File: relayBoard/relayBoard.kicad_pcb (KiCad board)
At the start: 4 copper layers, 220.7 x 245.6 mm, 517 parts, among them IC1 ADUM1251, J1 Conn_01x01, J10 Conn_02x04_Top_Bottom, J11 Conn_02x04_Top_Bottom, J12 Conn_02x04_Top_Bottom, J13 Conn_02x07_Odd_Even, J14 Conn_02x07_Odd_Even, J2 Conn_01x01, J3 Conn_01x01, J4 Conn_01x01, J5 Conn_01x01, J6 Conn_01x01, J7 Conn_02x04_Top_Bottom, J8 Conn_02x04_Top_Bottom, J9 Conn_02x04_Top_Bottom, K1 G6S-2 DC12, K10 G6S-2 DC12, K11 G6S-2 DC12, K12 G6S-2 DC12, K13 G6S-2 DC12, K14 G6S-2 DC12, K15 G6S-2 DC12, K16 G6S-2 DC12, K17 G6S-2 DC12, K18 G6S-2 DC12, K19 G6S-2 DC12, K2 G6S-2 DC12, K20 G6S-2 DC12, K21 G6S-2 DC12, K22 G6S-2 DC12, K23 G6S-2 DC12, K24 G6S-2 DC12, K25 G6S-2 DC12, K26 G6S-2 DC12, K27 G6S-2 DC12, K28 G6S-2 DC12, K29 G6S-2 DC12, K3 G6S-2 DC12, K30 G6S-2 DC12, K31 G6S-2 DC12, K32 G6S-2 DC12, K33 G6S-2 DC12, K34 G6S-2 DC12, K35 G6S-2 DC12, K36 G6S-2 DC12, K37 G6S-2 DC12, K38 G6S-2 DC12, K39 G6S-2 DC12, K4 G6S-2 DC12, K40 G6S-2 DC12, K41 G6S-2 DC12, K42 G6S-2 DC12, K43 CPC1777J, K44 CPC1777J, K45 CPC1777J, K46 CPC1777J, K47 CPC1777J, K48 CPC1777J, K49 CPC1777J, K5 G6S-2 DC12, K50 CPC1777J, K51 CPC1777J, K52 CPC1777J, K53 CPC1777J, K54 CPC1777J, K55 CPC1777J, K56 CPC1777J, K57 CPC1777J, K58 CPC1777J, K59 CPC1777J, K6 G6S-2 DC12, K60 CPC1777J, K61 CPC1777J, K62 CPC1777J, K63 CPC1777J, K7 G6S-2 DC12, K8 G6S-2 DC12, K9 G6S-2 DC12, Q1 2N7002, Q10 2N7002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

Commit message: Cuyler's revisions to the relay board
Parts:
- moved D148 19.4 mm to (107.8, -33.2), turned to 270 degrees
- moved C52 9.27 mm to (110.2, -37.5), turned to 90 degrees
- moved D149 9.18 mm to (108.1, -40.1), turned to 90 degrees
- moved R176 4.93 mm to (110.2, -40.5), turned to 90 degrees
- moved R177 4.77 mm to (150.6, -37.5)
- moved R178 4.75 mm to (152.1, -37.5)
- moved D150 4.71 mm to (150.8, -34.3), turned to 270 degrees
- moved C50 1.70 mm to (92.4, -37.1)
- moved R175 1.70 mm to (101.5, -34.3)
- moved U7 1.70 mm to (99.7, -38.4)
- moved C51 1.70 mm to (97.2, -34.3)
- moved R173 1.39 mm to (100.8, -41.8)
- moved U6 0.86 mm to (142.9, -37.8)
- moved R174 0.27 mm to (104.2, -37.6), turned to 270 degrees
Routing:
- net Net-(D149-Pad2): track 24.1 -> 4.22 mm
- net +12V: track 237.3 -> 225.2 mm, vias 95 -> 97
- net /INPUT_2: track 32.0 -> 28.4 mm
- net /Sheet5F711699/GATE_SUP: track 0.00 -> 3.36 mm
- net Net-(R177-Pad1): track 9.75 -> 6.98 mm
- net GND: track 466.1 -> 463.4 mm, vias 149 -> 151
- net Net-(D148-Pad1): track 6.55 -> 4.26 mm
- net Net-(R173-Pad2): track 4.05 -> 1.85 mm
- net Net-(C52-Pad2): track 3.45 -> 1.41 mm
- net Net-(R173-Pad1): track 13.5 -> 11.5 mm
- net Net-(D150-Pad1): track 2.65 -> 1.57 mm
- net Net-(R174-Pad1): track 2.76 -> 1.96 mm
- added copper zone on F.Cu, net Net-(D149-Pad2)
- added copper zone on F.Cu, net Net-(D150-Pad2)
- added copper zone on F.Cu, net Net-(D151-Pad2)
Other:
- board text added: "Cells 1-6"
- board text added: "Cells 13-18"
- board text added: "Cells 7-12"

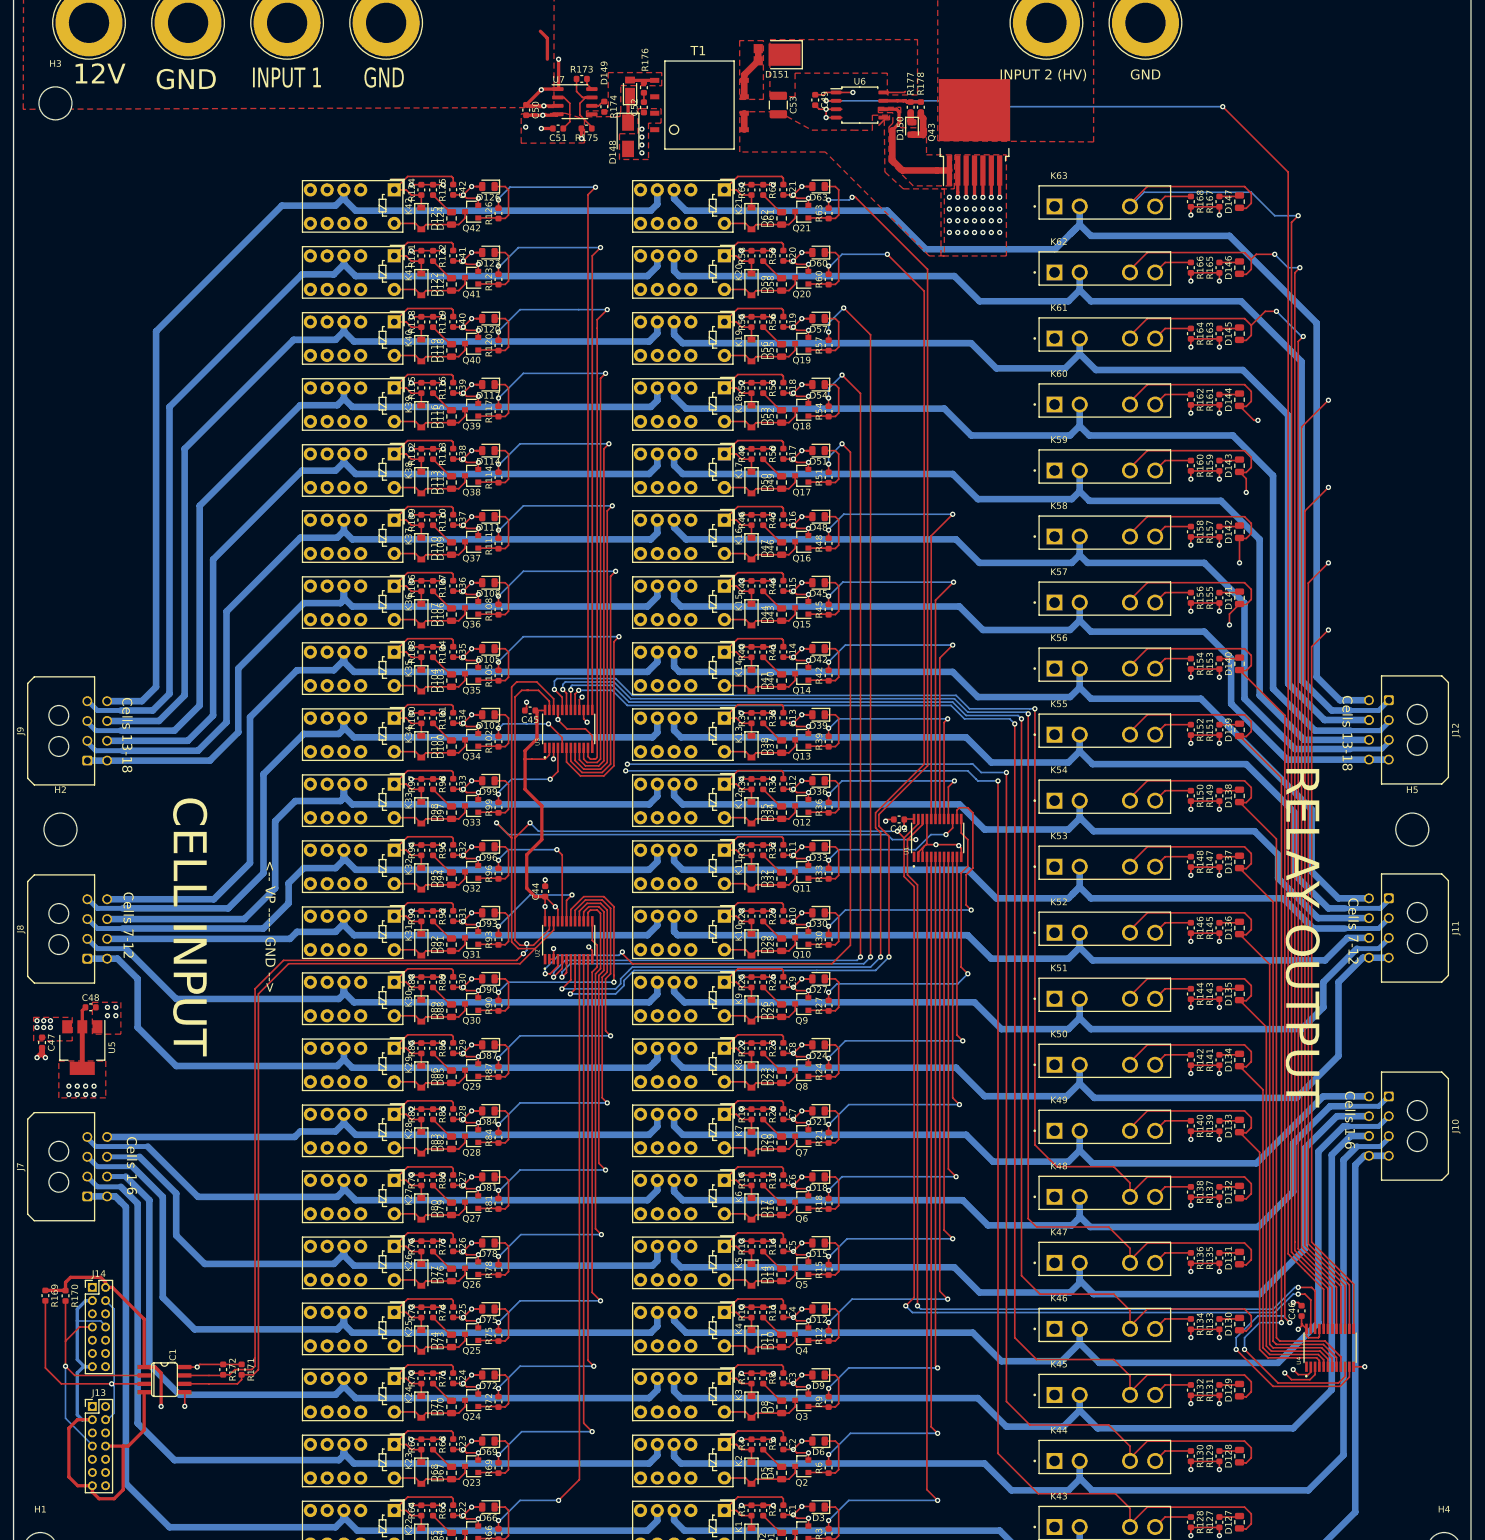
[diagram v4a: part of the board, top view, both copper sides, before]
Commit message: updates to connector connections and converter transformer
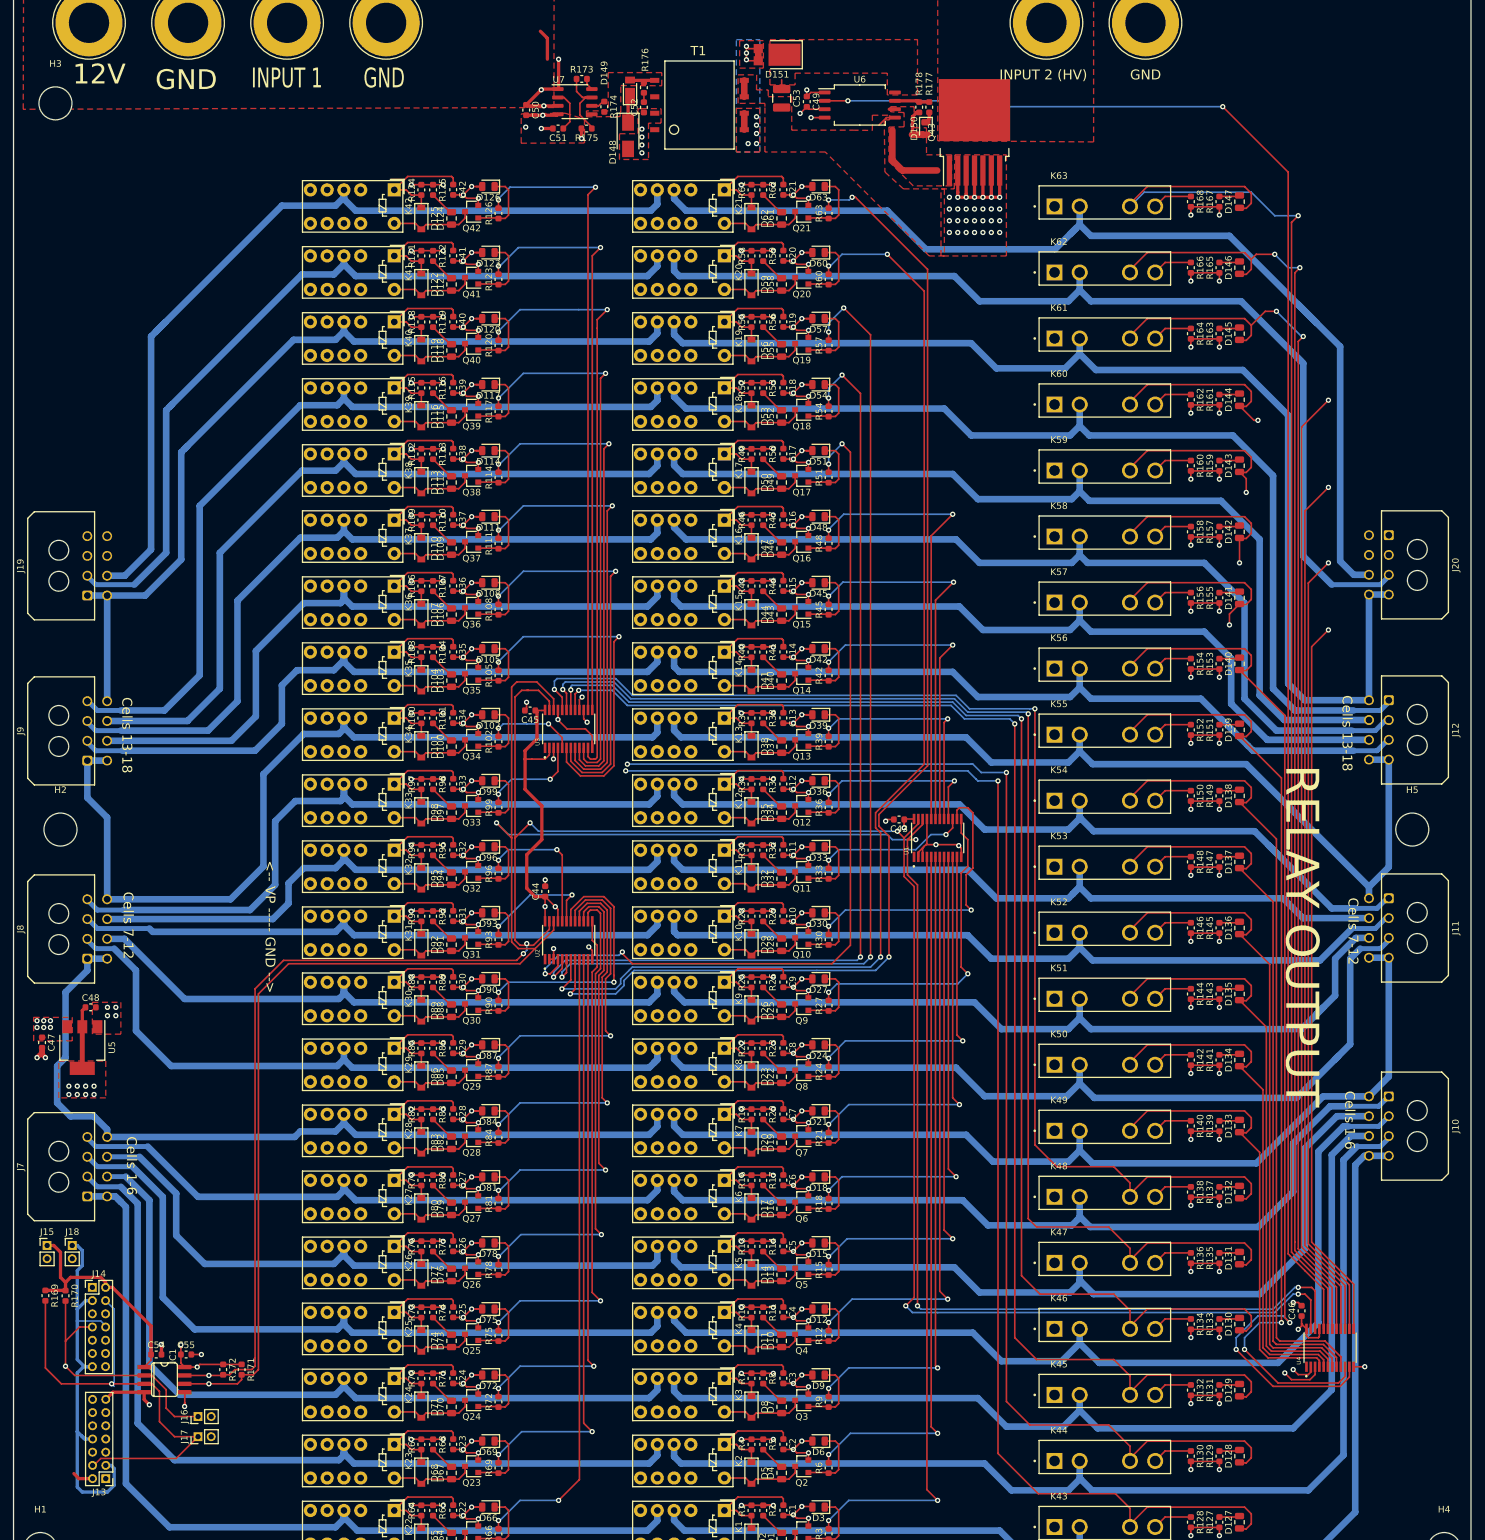
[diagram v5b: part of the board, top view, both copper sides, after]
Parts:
- added C54: 100n, Resistor_SMD:R_0603_1608Metric, F.Cu at (36.3, 151.4)
- added C55: 100n, Resistor_SMD:R_0603_1608Metric, F.Cu at (40.9, 151.4)
- added J15: Conn_01x02, Connector_PinHeader_2.00mm:PinHeader_1x02_P2.00mm_Vertical, F.Cu at (19.8, 134.9)
- added J16: Conn_01x02, Connector_PinHeader_2.00mm:PinHeader_1x02_P2.00mm_Vertical, F.Cu at (42.7, 160.8)
- added J17: Conn_01x02, Connector_PinHeader_2.00mm:PinHeader_1x02_P2.00mm_Vertical, F.Cu at (42.7, 163.8)
- added J18: Conn_01x02, Connector_PinHeader_2.00mm:PinHeader_1x02_P2.00mm_Vertical, F.Cu at (23.6, 134.9)
- added J19: Conn_02x04_Top_Bottom, Connector_Molex:Molex_Micro-Fit_3.0_43045-0800_2x04_P3.00mm_Horizontal, F.Cu at (25.9, 36.4)
- added J20: Conn_02x04_Top_Bottom, Connector_Molex:Molex_Micro-Fit_3.0_43045-0800_2x04_P3.00mm_Horizontal, F.Cu at (223.0, 27.3)
- C53: value 220u -> 10u
- T1: value 750313457 -> 750313445
- U6: footprint Package_SO:SOIC-8_5.23x5.23mm_P1.27mm -> Package_SO:SOIC-8_7.5x5.85mm_P1.27mm
- moved J13 11.1 mm to (28.7, 170.2), turned to 180 degrees
- moved R177 2.82 mm to (153.4, -37.5)
- moved D150 2.11 mm to (152.9, -34.3)
- moved C49 1.30 mm to (134.9, -38.4)
- moved C53 1.14 mm to (131.1, -38.9)
- moved R178 0.25 mm to (151.9, -37.5)
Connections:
- J11 pad 1: /OUT12 -> /OUT11
- J11 pad 2: /OUT10 -> /OUT9
- J11 pad 3: /OUT8 -> /OUT7
- J11 pad 4: /OUT7 -> /OUT6
- J11 pad 5: /OUT13 -> /OUT12
- J11 pad 6: /OUT11 -> /OUT10
- J11 pad 7: /OUT9 -> /OUT8
- J11 pad 8: /OUT7 -> /OUT6
- J12 pad 1: /OUT19 -> /OUT17
- J12 pad 2: /OUT17 -> /OUT15
- J12 pad 3: /OUT15 -> /OUT13
- J12 pad 4: /OUT14 -> /OUT12
- J12 pad 5: /OUT20 -> /OUT18
- J12 pad 6: /OUT18 -> /OUT16
- J12 pad 7: /OUT16 -> /OUT14
- J12 pad 8: /OUT14 -> /OUT12
- J8 pad 1: /IN7 -> /IN6
- J8 pad 2: /IN8 -> /IN7
- J8 pad 3: /IN10 -> /IN9
- J8 pad 4: /IN12 -> /IN11
- J8 pad 5: /IN7 -> /IN6
- J8 pad 6: /IN9 -> /IN8
- J8 pad 7: /IN11 -> /IN10
- J8 pad 8: /IN13 -> /IN12
- J9 pad 1: /IN14 -> /IN12
- J9 pad 2: /IN15 -> /IN13
- J9 pad 3: /IN17 -> /IN15
- J9 pad 4: /IN19 -> /IN17
- J9 pad 5: /IN14 -> /IN12
- J9 pad 6: /IN16 -> /IN14
- J9 pad 7: /IN18 -> /IN16
- J9 pad 8: /IN20 -> /IN18
- Q43 pad 3: /INPUT_2 -> (no net)
- Q43 pad 4: /INPUT_2 -> (no net)
- Q43 pad 5: /INPUT_2 -> (no net)
- Q43 pad 6: /INPUT_2 -> (no net)
- Q43 pad 7: /INPUT_2 -> (no net)
- T1 pad 5: Net-(D151-Pad2) -> /INPUT_2
- T1 pad 6: Net-(D151-Pad2) -> /INPUT_2
- T1 pad 7: /INPUT_2 -> Net-(D151-Pad2)
- T1 pad 8: /INPUT_2 -> Net-(D151-Pad2)
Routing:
- net /IN6: track 88.6 -> 125.8 mm
- net /Sheet5F711418/5V_2: track 43.3 -> 77.3 mm, vias 1 -> 0
- net /Sheet5F711418/SCL_2: track 45.9 -> 72.0 mm
- net /OUT6: track 117.9 -> 143.2 mm
- net /IN12: track 113.1 -> 133.6 mm
- net /IN19: track 144.5 -> 124.4 mm
- net /IN20: track 152.3 -> 133.7 mm
- net /OUT18: track 159.3 -> 177.0 mm
- net /OUT19: track 171.1 -> 153.4 mm
- net /Sheet5F711418/GND_2: track 71.0 -> 88.3 mm, vias 0 -> 2
- net /OUT20: track 176.5 -> 160.3 mm
- net /OUT12: track 131.5 -> 147.7 mm
- net /IN13: track 116.7 -> 101.6 mm
- net /Sheet5F711418/SDA_2: track 41.1 -> 55.1 mm
- net /Sheet5F711418/SCL: track 383.6 -> 395.3 mm, vias 4 -> 5
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- added copper zone on B.Cu, net Net-(D151-Pad2)
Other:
- board text removed: "CELL INPUT"
